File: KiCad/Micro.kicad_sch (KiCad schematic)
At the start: 25 parts, among them J1 Conn_01x02, J1 DE9_Pins, J2 DE9_Pins, J3 Conn_01x05, SW1 SW_Push, U1 MCP4725xxx-xCH, U1 PIC24HJ128GP502, U2 MCP2562-E-SN, U3 MAX3232, Y1 Crystal

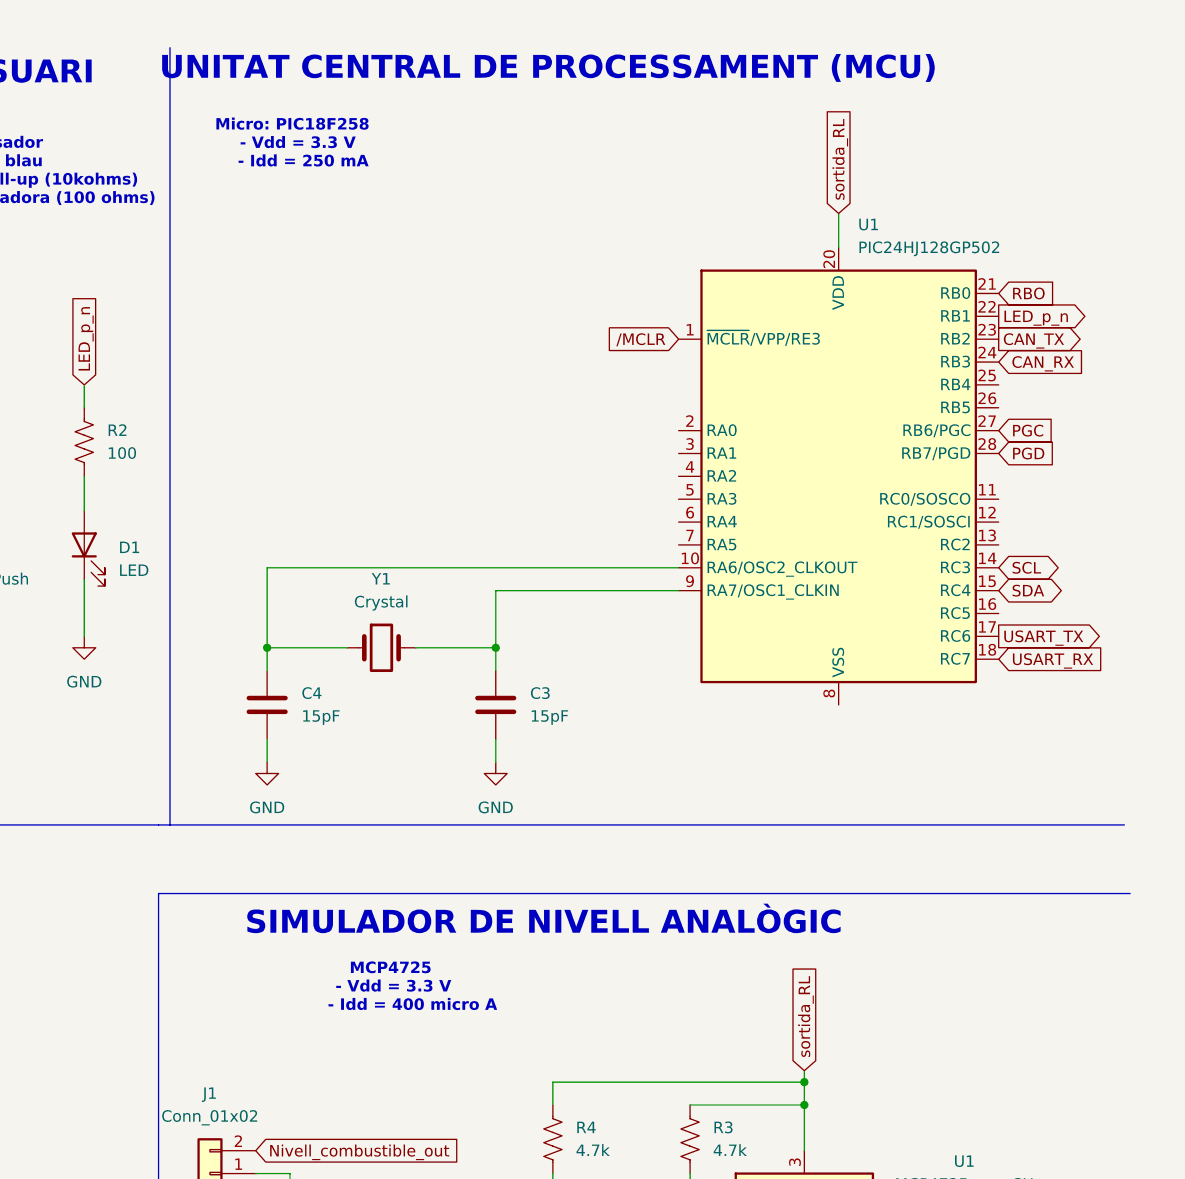
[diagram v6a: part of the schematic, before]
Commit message: Arreglat els pins i cambiat el model del relé
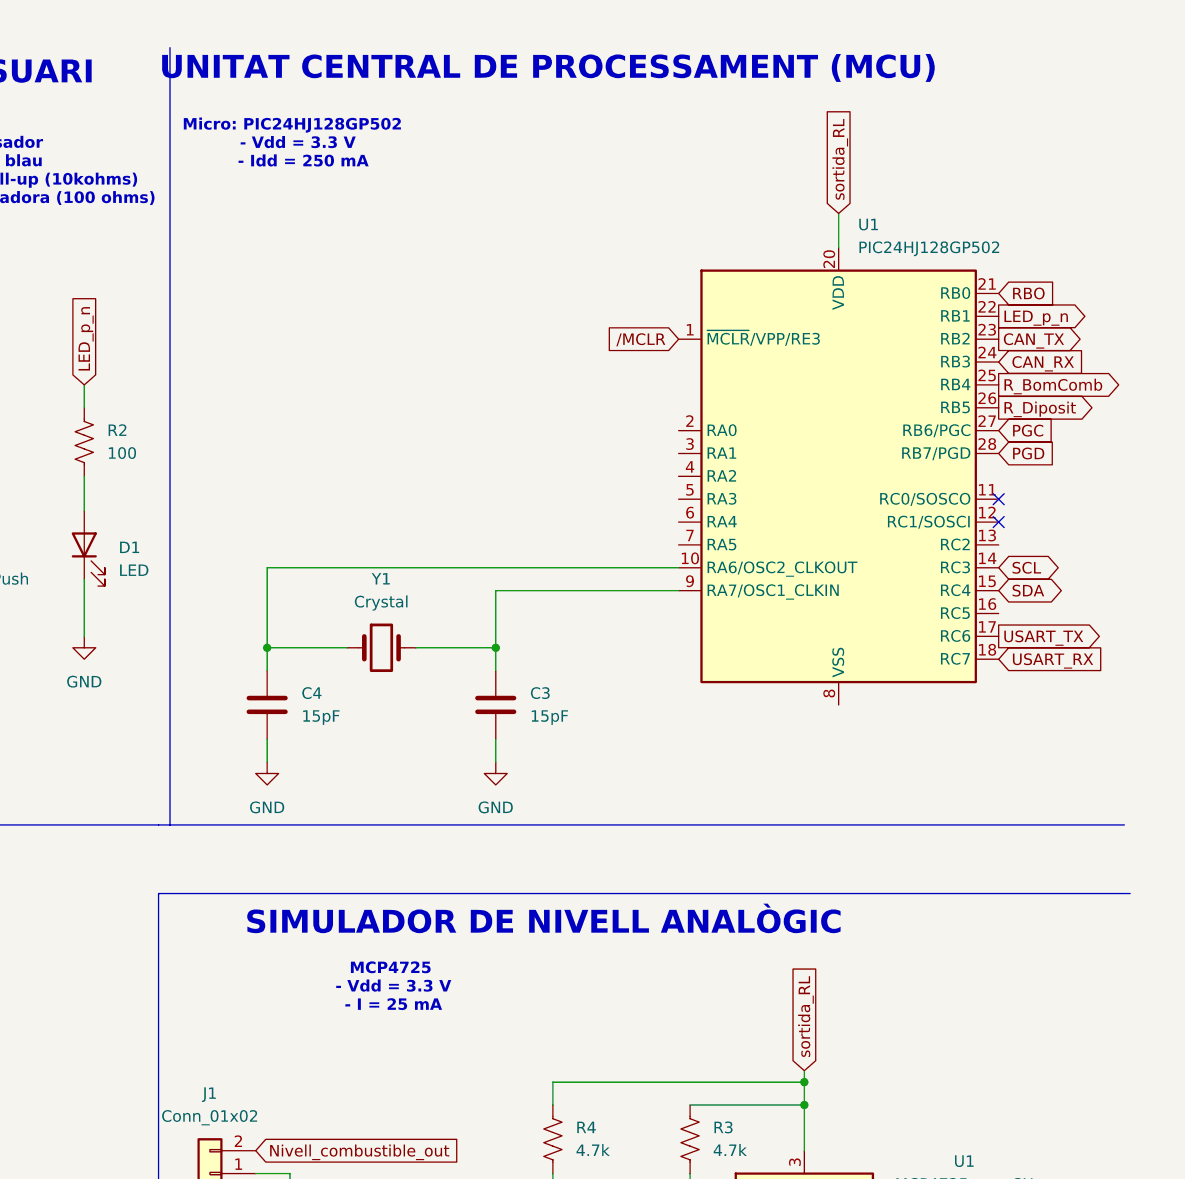
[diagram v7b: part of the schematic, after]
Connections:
- net R_BomComb: now reaches U1.25 (RB4)
- net R_Diposit: now reaches U1.26 (RB5)
- no-connect marks 18 -> 20
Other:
- note added: "MCP4725 - Vdd = 3.3 V - I = 25 mA"
- note added: "Micro: PIC24HJ128GP502 - Vdd = 3.3 V - Idd = 250 mA"
- note removed: "MCP4725 - Vdd = 3.3 V - Idd = 400 micro A"
- note removed: "Micro: PIC18F258 - Vdd = 3.3 V - Idd = 250 mA"
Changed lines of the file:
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@@
 		)
 	)
-	(text "MCP4725\n - Vdd = 3.3 V\n        - Idd = 400 micro A"
+	(text "MCP4725\n - Vdd = 3.3 V\n - I = 25 mA"
 		(exclude_from_sim no)
 		(at 202.946 117.856 0)
@@
 		)
 	)
-	(text "Micro: PIC18F258 \n  - Vdd = 3.3 V\n    - Idd = 250 mA"
+	(text "Micro: PIC24HJ128GP502 \n  - Vdd = 3.3 V\n    - Idd = 250 mA"
 		(exclude_from_sim no)
 		(at 192.024 24.13 0)
@@
 	)
 	(no_connect
+		(at 270.51 63.5)
+	)
+	(no_connect
 		(at 30.48 57.15)
 	)
@@
 	)
 	(no_connect
+		(at 270.51 66.04)
+	)
+	(no_connect
 		(at 30.48 54.61)
 	)
@@
 			(width 0)
 			(type default)
+		)
+	)
+	(global_label "R_Diposit"
+		(shape output)
+		(at 270.51 53.34 0)
+		(fields_autoplaced yes)
+		(effects
+			(font
+				(size 1.27 1.27)
+			)
+			(justify left)
+		)
+		(property "Intersheetrefs" "${INTERSHEET_REFS}"
+			(at 282.2642 53.34 0)
+			(effects
+				(font
+					(size 1.27 1.27)
+				)
+				(justify left)
+				(hide yes)
+			)
 		)
 	)
@@
 			(effects
 				(font
+					(size 1.27 1.27)
+				)
+				(justify left)
+				(hide yes)
+			)
+		)
+	)
+	(global_label "R_BomComb"
+		(shape output)
+		(at 270.51 50.8 0)
+		(fields_autoplaced yes)
+		(effects
+			(font
+				(size 1.27 1.27)
+			)
+			(justify left)
+		)
+		(property "Intersheetrefs" "${INTERSHEET_REFS}"
+			(at 285.1064 50.8 0)
+			(effects
+				(font
